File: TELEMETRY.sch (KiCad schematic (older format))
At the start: 3 parts, among them U9 RFM95W-868S2, X2 SMACONNECTOR

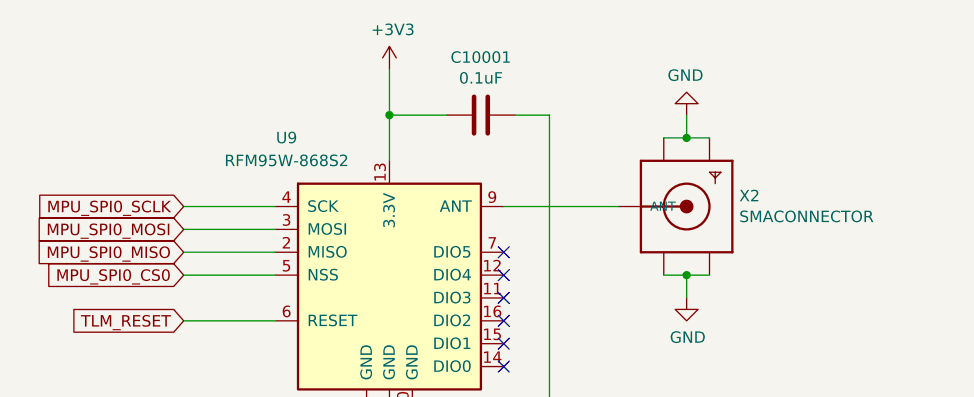
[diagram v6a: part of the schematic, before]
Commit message: added minecraft with shaders (jetson nano) + switched to Teensy 4.1
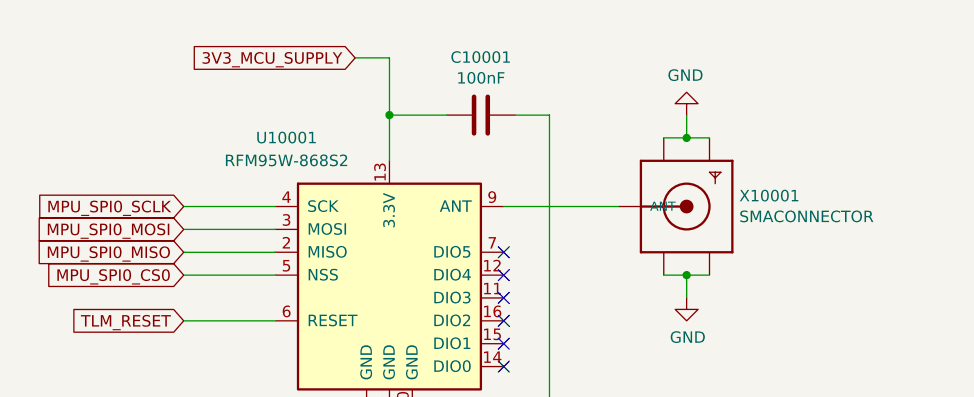
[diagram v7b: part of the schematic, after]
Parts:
- C10001: value 0.1uF -> 100nF
- renumbered U9 to U10001, X2 to X10001
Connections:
- net +3V3 renamed 3V3_MCU_SUPPLY
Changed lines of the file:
@@
 $Descr A4 11693 8268
 encoding utf-8
-Sheet 10 10
+Sheet 10 11
 Title "TARS-MK1"
 Date ""
@@
 $EndDescr
 $Comp
-L ISS_LOGO:LOGO #G9
+L ISS_LOGO:LOGO #G10001
 U 1 1 5F87BCA1
 P 7600 6800
-F 0 "#G9" H 7600 6677 60  0001 C CNN
+F 0 "#G10001" H 7600 6677 60  0001 C CNN
 F 1 "LOGO" H 7600 6923 60  0001 C CNN
 F 2 "" H 7600 6800 50  0001 C CNN
@@
 $EndComp
 $Comp
-L power:GND #PWR020
+L power:GND #PWR010001
 U 1 1 5F947841
 P 3500 3800
-F 0 "#PWR020" H 3500 3550 50  0001 C CNN
+F 0 "#PWR010001" H 3500 3550 50  0001 C CNN
 F 1 "GND" H 3505 3627 50  0000 C CNN
 F 2 "" H 3500 3800 50  0001 C CNN
@@
 	4000 2650 4500 2650
 $Comp
-L power:GND #PWR022
+L power:GND #PWR010003
 U 1 1 5F949889
 P 4800 3050
-F 0 "#PWR022" H 4800 2800 50  0001 C CNN
+F 0 "#PWR010003" H 4800 2800 50  0001 C CNN
 F 1 "GND" H 4805 2877 50  0000 C CNN
 F 2 "" H 4800 3050 50  0001 C CNN
@@
 	4800 2950 4900 2950
 $Comp
-L power:GND #PWR021
+L power:GND #PWR010002
 U 1 1 5F949FA5
 P 4800 2250
-F 0 "#PWR021" H 4800 2000 50  0001 C CNN
+F 0 "#PWR010002" H 4800 2000 50  0001 C CNN
 F 1 "GND" H 4805 2077 50  0000 C CNN
 F 2 "" H 4800 2250 50  0001 C CNN
@@
 	4800 2350 4900 2350
 $Comp
-L SMA:SMACONNECTOR X2
+L SMA:SMACONNECTOR X10001
 U 1 1 5F94DDFD
 P 4800 2650
-F 0 "X2" H 5030 2696 50  0000 L CNN
+F 0 "X10001" H 5030 2696 50  0000 L CNN
 F 1 "SMACONNECTOR" H 5030 2605 50  0000 L CNN
 F 2 "SMA:SMA90_DIP" H 4800 2650 50  0001 C CNN
@@
 $EndComp
 $Comp
-L power:+3V3 #PWR0134
-U 1 1 5F98F509
-P 3500 2050
-F 0 "#PWR0134" H 3500 1900 50  0001 C CNN
-F 1 "+3V3" H 3515 2223 50  0000 C CNN
-F 2 "" H 3500 2050 50  0001 C CNN
-F 3 "" H 3500 2050 50  0001 C CNN
-	1    3500 2050
-	1    0    0    -1
-$EndComp
-Wire Wire Line
-	3500 2050 3500 2250
-$Comp
 L D24V50F5:C C10001
 U 1 1 5F991F8E
 P 3900 2250
 F 0 "C10001" V 3648 2250 50  0000 C CNN
-F 1 "0.1uF" V 3739 2250 50  0000 C CNN
+F 1 "100nF" V 3739 2250 50  0000 C CNN
 F 2 "" H 3938 2100 50  0001 C CNN
 F 3 "~" H 3900 2250 50  0001 C CNN
@@
 	4200 3650 3600 3650
 $Comp
-L RF_Module:RFM95W-868S2 U9
+L RF_Module:RFM95W-868S2 U10001
 U 1 1 5F8B4512
 P 3500 2950
-F 0 "U9" H 3050 3550 50  0000 C CNN
+F 0 "U10001" H 3050 3550 50  0000 C CNN
 F 1 "RFM95W-868S2" H 3050 3450 50  0000 C CNN
 F 2 "" H 200 4600 50  0001 C CNN
@@
 Wire Wire Line
 	2600 3150 3000 3150
+Text GLabel 3350 2000 0    50   Input ~ 0
+3V3_MCU_SUPPLY
+Wire Wire Line
+	3500 2000 3350 2000
+Wire Wire Line
+	3500 2000 3500 2250
 $EndSCHEMATC
